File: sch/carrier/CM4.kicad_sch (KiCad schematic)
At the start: 11 parts

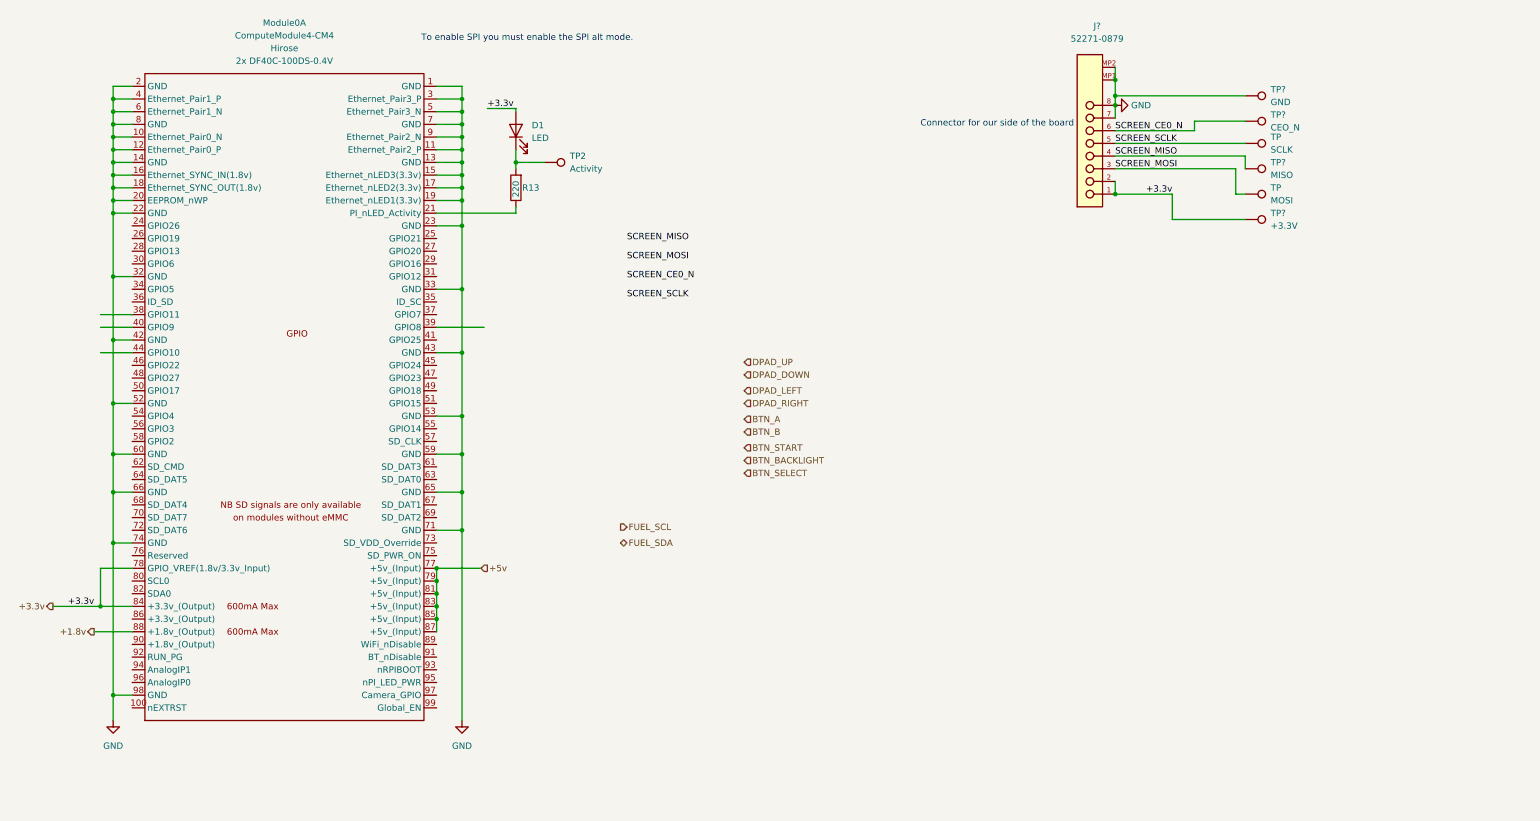
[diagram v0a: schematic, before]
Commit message: add speaker and charger
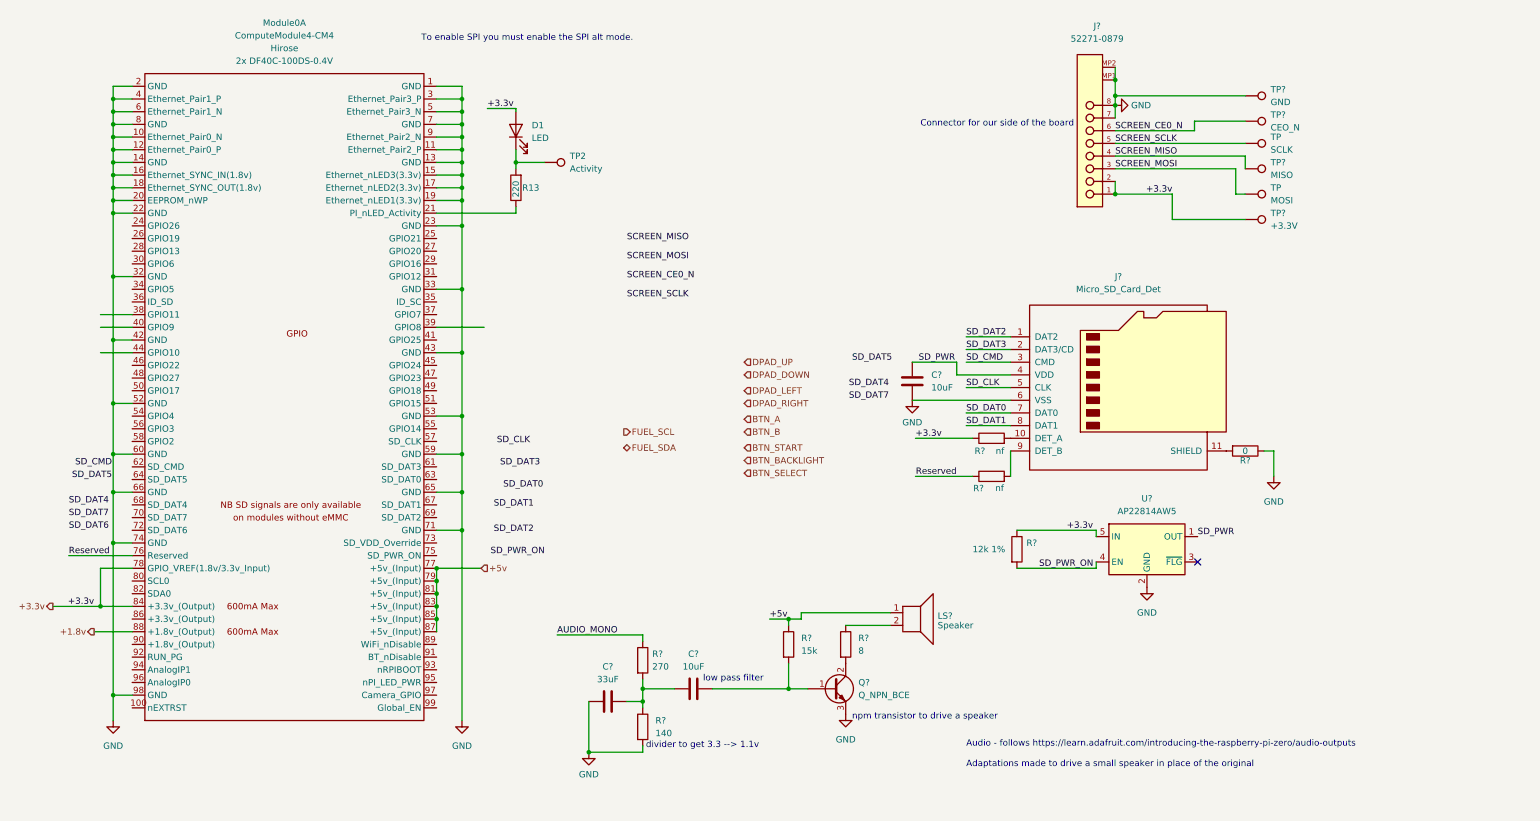
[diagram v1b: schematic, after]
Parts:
- added C?: 33uF, symbol Device:C
- added C? (x2): 10uF, symbol Device:C
- added J?: Micro_SD_Card_Det, sdcard:HRS_DM3CS-SF, symbol Connector:Micro_SD_Card_Det
- added LS?: Speaker, symbol Device:Speaker
- added Q?: Q_NPN_BCE, symbol Device:Q_NPN_BCE
- added R?: 12k 1%, symbol Device:R
- added R?: 15k, symbol Device:R
- added R?: 270, symbol Device:R
- added R?: 0, symbol Device:R
- added R?: 8, symbol Device:R
- added R? (x2): nf, Resistor_SMD:R_0402_1005Metric, symbol Device:R
- added R?: 140, symbol Device:R
- added U?: AP22814AW5, Package_TO_SOT_SMD:SOT-23-5, symbol Power_Management:AP22814AW5
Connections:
- net +3.3v: now also R?.1, R?.1, U?.5 (IN)
- net +5v: now also LS?.1, R?.1
- net GND: now also C?.1, C?.2, J?.6 (VSS), Q?.3 (E), R?.1, R?.2, U?.2 (GND)
- net Reserved: now reaches Module0.76 (Reserved)
- net Reserved: now also R?.1
- new net: C?.2, Q?.1 (B), R?.2
- new net: C?.1, C?.2, R?.1, R?.2
- new net: J?.11 (SHIELD), R?.2
- new net: LS?.2, R?.1
- new net: Q?.2 (C), R?.2
- new net: J?.10 (DET_A), R?.2
- new net: J?.9 (DET_B), R?.2
- new net AUDIO_MONO: R?.1
- new net SD_CLK: J?.5 (CLK)
- new net SD_CMD: J?.3 (CMD)
- new net SD_DAT0: J?.7 (DAT0)
- new net SD_DAT1: J?.8 (DAT1)
- new net SD_DAT2: J?.1 (DAT2)
- new net SD_DAT3: J?.2 (DAT3/CD)
- new net SD_PWR: C?.1, J?.4 (VDD), U?.1 (OUT)
- new net SD_PWR_ON: R?.2, U?.4 (EN)
- no-connect marks 0 -> 1
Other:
- note added: "Audio - follows https://learn.adafruit.com/introducing-the-raspberry-pi-zero/audio-outputs Adaptations made to drive a small speaker in place of the original"
- note added: "divider to get 3.3 --> 1.1v"
- note added: "low pass filter"
- note added: "npm transistor to drive a speaker"

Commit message: push updates
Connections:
- net AUDIO_MONO: no longer R?.1
- net FUEL_SCL: now also Module0.80 (SCL0)
- net FUEL_SDA: now also Module0.82 (SDA0)
- net SCREEN_CE0_N: now also Module0.39 (GPIO8)
- net SCREEN_MISO: now also Module0.40 (GPIO9)
- net SCREEN_MOSI: now also Module0.44 (GPIO10)
- net SCREEN_SCLK: now also Module0.38 (GPIO11)
- net SD_CLK: now also Module0.57 (SD_CLK)
- net SD_CMD: now also Module0.62 (SD_CMD)
- net SD_DAT0: now also Module0.63 (SD_DAT0)
- net SD_DAT1: now also Module0.67 (SD_DAT1)
- net SD_DAT2: now also Module0.69 (SD_DAT2)
- net SD_DAT3: now also Module0.61 (SD_DAT3)
- net SD_PWR_ON: now also Module0.75 (SD_PWR_ON)
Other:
- note added: "Display connector for our side"
- note removed: "Connector for our side of the board"
- moved on the sheet: C?, J?, LS?, Q?, R?, TP, TP?, U?

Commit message: adsasdas
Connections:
- net AUDIO_MONO: now also R?.1
- net BTN_A: now also Module0.49 (GPIO18)
- net BTN_B: now also Module0.29 (GPIO16)
- net BTN_BACKLIGHT: now also Module0.27 (GPIO20)
- net BTN_SELECT: now also Module0.25 (GPIO21)
- net BTN_START: now also Module0.26 (GPIO19)
- net DPAD_DOWN: now also Module0.55 (GPIO14)
- net DPAD_LEFT: now also Module0.28 (GPIO13)
- net DPAD_RIGHT: now also Module0.31 (GPIO12)
- net DPAD_UP: now also Module0.50 (GPIO17)
- net GLOBAL_EN: now reaches Module0.99 (Global_EN)
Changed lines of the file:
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@@
+    (stroke (width 0) (type solid) (color 0 0 0 0))
+  )
+  (wire (pts (xy 29.845 58.42) (xy 35.56 58.42))
+    (stroke (width 0) (type solid) (color 0 0 0 0))
+  )
+  (wire (pts (xy 29.845 60.96) (xy 35.56 60.96))
+    (stroke (width 0) (type solid) (color 0 0 0 0))
+  )
+  (wire (pts (xy 29.845 88.9) (xy 35.56 88.9))
     (stroke (width 0) (type solid) (color 0 0 0 0))
   )
@@
     (stroke (width 0) (type solid) (color 0 0 0 0))
   )
+  (wire (pts (xy 96.52 58.42) (xy 103.505 58.42))
+    (stroke (width 0) (type solid) (color 0 0 0 0))
+  )
+  (wire (pts (xy 96.52 60.96) (xy 103.505 60.96))
+    (stroke (width 0) (type solid) (color 0 0 0 0))
+  )
+  (wire (pts (xy 96.52 63.5) (xy 103.505 63.5))
+    (stroke (width 0) (type solid) (color 0 0 0 0))
+  )
+  (wire (pts (xy 96.52 66.04) (xy 103.505 66.04))
+    (stroke (width 0) (type solid) (color 0 0 0 0))
+  )
   (wire (pts (xy 96.52 68.58) (xy 101.6 68.58))
     (stroke (width 0) (type solid) (color 0 0 0 0))
@@
     (stroke (width 0) (type solid) (color 0 0 0 0))
   )
+  (wire (pts (xy 96.52 88.9) (xy 103.505 88.9))
+    (stroke (width 0) (type solid) (color 0 0 0 0))
+  )
   (wire (pts (xy 96.52 93.98) (xy 101.6 93.98))
     (stroke (width 0) (type solid) (color 0 0 0 0))
   )
+  (wire (pts (xy 96.52 96.52) (xy 103.505 96.52))
+    (stroke (width 0) (type solid) (color 0 0 0 0))
+  )
   (wire (pts (xy 96.52 99.06) (xy 109.855 99.06))
     (stroke (width 0) (type solid) (color 0 0 0 0))
@@
     (stroke (width 0) (type solid) (color 0 0 0 0))
   )
+  (wire (pts (xy 96.52 152.4) (xy 103.505 152.4))
+    (stroke (width 0) (type solid) (color 0 0 0 0))
+  )
   (wire (pts (xy 101.6 27.94) (xy 101.6 30.48))
     (stroke (width 0) (type solid) (color 0 0 0 0))
@@
     (stroke (width 0) (type solid) (color 0 0 0 0))
   )
-  (wire (pts (xy 120.65 137.795) (xy 137.795 137.795))
+  (wire (pts (xy 191.135 137.16) (xy 208.28 137.16))
     (stroke (width 0) (type solid) (color 0 0 0 0))
   )
@@
     (effects (font (size 1.27 1.27)) (justify right bottom))
   )
-  (label "AUDIO_MONO" (at 120.65 137.795 0)
+  (label "AUDIO_MONO" (at 191.135 137.16 0)
     (effects (font (size 1.27 1.27)) (justify left bottom))
   )
@@
     (effects (font (size 1.27 1.27)) (justify right))
   )
-  (hierarchical_label "BTN_START" (shape input) (at 29.21 58.42 180)
+  (hierarchical_label "BTN_START" (shape input) (at 29.845 58.42 180)
     (effects (font (size 1.27 1.27)) (justify right))
   )
-  (hierarchical_label "DPAD_LEFT" (shape input) (at 29.21 60.96 180)
+  (hierarchical_label "DPAD_LEFT" (shape input) (at 29.845 60.96 180)
     (effects (font (size 1.27 1.27)) (justify right))
   )
@@
     (effects (font (size 1.27 1.27)) (justify right))
   )
+  (hierarchical_label "BTN_SELECT" (shape input) (at 103.505 58.42 0)
+    (effects (font (size 1.27 1.27)) (justify left))
+  )
+  (hierarchical_label "BTN_BACKLIGHT" (shape input) (at 103.505 60.96 0)
+    (effects (font (size 1.27 1.27)) (justify left))
+  )
+  (hierarchical_label "BTN_B" (shape input) (at 103.505 63.5 0)
+    (effects (font (size 1.27 1.27)) (justify left))
+  )
+  (hierarchical_label "DPAD_RIGHT" (shape input) (at 103.505 66.04 0)
+    (effects (font (size 1.27 1.27)) (justify left))
+  )
   (hierarchical_label "BTN_A" (shape input) (at 103.505 88.9 0)
     (effects (font (size 1.27 1.27)) (justify left))
   )
-  (hierarchical_label "BTN_SELECT" (shape input) (at 104.14 59.055 0)
+  (hierarchical_label "DPAD_DOWN" (shape input) (at 103.505 96.52 0)
     (effects (font (size 1.27 1.27)) (justify left))
   )
-  (hierarchical_label "BTN_BACKLIGHT" (shape input) (at 104.14 60.96 0)
+  (hierarchical_label "GLOBAL_EN" (shape output) (at 103.505 152.4 0)
     (effects (font (size 1.27 1.27)) (justify left))
   )
-  (hierarchical_label "BTN_B" (shape input) (at 104.14 63.5 0)
-    (effects (font (size 1.27 1.27)) (justify left))
-  )
-  (hierarchical_label "DPAD_RIGHT" (shape input) (at 104.14 66.04 0)
-    (effects (font (size 1.27 1.27)) (justify left))
-  )
-  (hierarchical_label "DPAD_DOWN" (shape input) (at 104.14 96.52 0)
-    (effects (font (size 1.27 1.27)) (justify left))
-  )

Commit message: aaaaaaaaaaaaaa
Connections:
- net SHOULDER_L: now reaches Module0.46 (GPIO22)
- net SHOULDER_R: now reaches Module0.47 (GPIO23)
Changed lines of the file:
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@@
+    (stroke (width 0) (type solid) (color 0 0 0 0))
+  )
+  (wire (pts (xy 31.115 83.82) (xy 35.56 83.82))
     (stroke (width 0) (type solid) (color 0 0 0 0))
   )
@@
   )
   (wire (pts (xy 96.52 81.28) (xy 101.6 81.28))
+    (stroke (width 0) (type solid) (color 0 0 0 0))
+  )
+  (wire (pts (xy 96.52 86.36) (xy 103.505 86.36))
     (stroke (width 0) (type solid) (color 0 0 0 0))
   )
@@
     (effects (font (size 1.27 1.27)) (justify right))
   )
+  (hierarchical_label "SHOULDER_L" (shape input) (at 31.115 83.82 180)
+    (effects (font (size 1.27 1.27)) (justify right))
+  )
   (hierarchical_label "BTN_SELECT" (shape input) (at 103.505 58.42 0)
     (effects (font (size 1.27 1.27)) (justify left))
@@
     (effects (font (size 1.27 1.27)) (justify left))
   )
+  (hierarchical_label "SHOULDER_R" (shape input) (at 103.505 86.36 0)
+    (effects (font (size 1.27 1.27)) (justify left))
+  )

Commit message: ersfdxcv
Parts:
- TP1: renamed from TP?; footprint TestPoint:TestPoint_Pad_2.0x2.0mm -> TestPoint:TestPoint_Pad_1.0x1.0mm
- TP12, TP4: renamed from TP; footprint (none) -> TestPoint:TestPoint_Pad_1.0x1.0mm
- TP13, TP3, TP5: renamed from TP?; footprint (none) -> TestPoint:TestPoint_Pad_1.0x1.0mm
- TP2: footprint TestPoint:TestPoint_Pad_2.0x2.0mm -> TestPoint:TestPoint_Pad_1.0x1.0mm
- gave numbers to parts that had none: 16

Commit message: footprint assignmnt
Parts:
- R13: footprint Resistor_SMD:R_0805_2012Metric_Pad1.20x1.40mm_HandSolder -> Capacitor_SMD:C_0402_1005Metric_Pad0.74x0.62mm_HandSolder
- R22: footprint (none) -> Resistor_SMD:R_0402_1005Metric_Pad0.72x0.64mm_HandSolder
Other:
- note added: "close relative part to whats on the cm4io's sheet"
- note added: "not sure what this is for, thanks Pi Foundation for making a nf resistor for a pin we don't know what it does! (notetoself: nf means do not connect)"
- note added: "our signal output is apparently a PWM (digital thingymajigy) will 'trick the speaker'"
- note added: "pullup ensure default on"
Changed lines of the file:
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@@
     (effects (font (size 1.27 1.27)) (justify right bottom))
+  )
+  (text "our signal output is apparently a PWM (digital thingymajigy)\nwill 'trick the speaker'"
+    (at 175.26 133.985 0)
+    (effects (font (size 1.27 1.27)) (justify left bottom))
   )
   (text "Audio - follows https://learn.adafruit.com/introducing-the-raspberry-pi-zero/audio-outputs\n\nAdaptations made to drive a small speaker in place of the original"
@@
     (effects (font (size 1.27 1.27)) (justify left bottom))
   )
+  (text "not sure what this is for, thanks Pi Foundation for \nmaking a nf resistor for a pin we don't know what it does!\n(notetoself: nf means do not connect)"
+    (at 181.61 100.33 0)
+    (effects (font (size 0.762 0.762)) (justify left bottom))
+  )
+  (text "pullup ensure default on\n" (at 206.375 107.315 0)
+    (effects (font (size 1.27 1.27)) (justify left bottom))
+  )
   (text "divider to get 3.3 --> 1.1v" (at 208.915 160.02 0)
     (effects (font (size 1.27 1.27)) (justify left bottom))
   )
   (text "low pass filter" (at 220.345 146.685 0)
+    (effects (font (size 1.27 1.27)) (justify left bottom))
+  )
+  (text "close relative part to whats on the cm4io's sheet\n"
+    (at 234.95 125.095 0)
     (effects (font (size 1.27 1.27)) (justify left bottom))
   )
@@
       (effects (font (size 1.27 1.27)) (justify right))
     )
-    (property "Footprint" "Resistor_SMD:R_0805_2012Metric_Pad1.20x1.40mm_HandSolder" (id 2) (at 114.173 48.26 90)
+    (property "Footprint" "Capacitor_SMD:C_0402_1005Metric_Pad0.74x0.62mm_HandSolder" (id 2) (at 114.173 48.26 90)
       (effects (font (size 1.27 1.27)) hide)
     )
@@
       (effects (font (size 1.27 1.27)) (justify left))
     )
-    (property "Footprint" "" (id 2) (at 229.997 109.855 90)
-      (effects (font (size 1.27 1.27)) hide)
-    )
+    (property "Footprint" "Resistor_SMD:R_0402_1005Metric_Pad0.72x0.64mm_HandSolder" (id 2) (at 229.997 109.855 90)
+      (effects (font (size 1.27 1.27)) hide)
+    )

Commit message: a
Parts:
- R14, R18, R23, R24: footprint (none) -> Resistor_SMD:R_0603_1608Metric_Pad0.98x0.95mm_HandSolder
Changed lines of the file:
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@@
       (effects (font (size 1.27 1.27)) (justify left))
     )
-    (property "Footprint" "" (id 2) (at 206.502 142.24 90)
+    (property "Footprint" "Resistor_SMD:R_0603_1608Metric_Pad0.98x0.95mm_HandSolder" (id 2) (at 206.502 142.24 90)
       (effects (font (size 1.27 1.27)) hide)
     )
@@
       (effects (font (size 1.27 1.27)) (justify left))
     )
-    (property "Footprint" "" (id 2) (at 206.502 155.575 90)
+    (property "Footprint" "Resistor_SMD:R_0603_1608Metric_Pad0.98x0.95mm_HandSolder" (id 2) (at 206.502 155.575 90)
       (effects (font (size 1.27 1.27)) hide)
     )
@@
       (effects (font (size 1.27 1.27)) (justify left))
     )
-    (property "Footprint" "" (id 2) (at 235.712 139.065 90)
+    (property "Footprint" "Resistor_SMD:R_0603_1608Metric_Pad0.98x0.95mm_HandSolder" (id 2) (at 235.712 139.065 90)
       (effects (font (size 1.27 1.27)) hide)
     )
@@
       (effects (font (size 1.27 1.27)) (justify left))
     )
-    (property "Footprint" "" (id 2) (at 247.142 139.065 90)
+    (property "Footprint" "Resistor_SMD:R_0603_1608Metric_Pad0.98x0.95mm_HandSolder" (id 2) (at 247.142 139.065 90)
       (effects (font (size 1.27 1.27)) hide)
     )
